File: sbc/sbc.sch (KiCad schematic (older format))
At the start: 15 parts, among them J1 Conn_01x11_Female, J2 Conn_01x11_Female, U1 WD65C02, U2 7400, U3 28C256, U4 HM62256BLP, U5 WD65C22

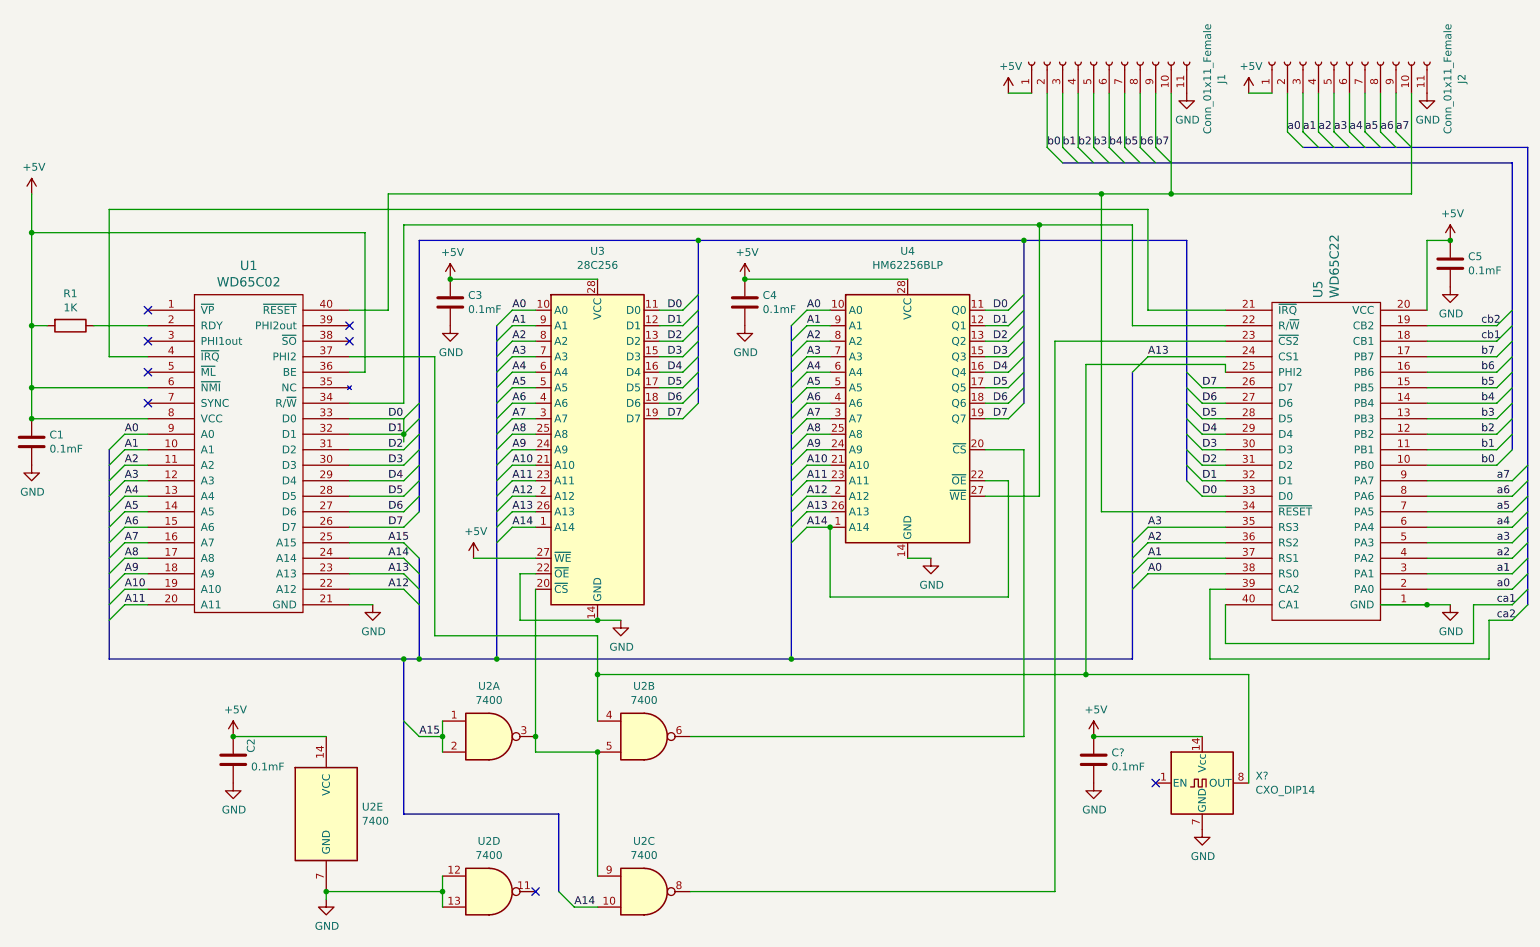
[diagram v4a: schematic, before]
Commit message: SBC: Power and reset
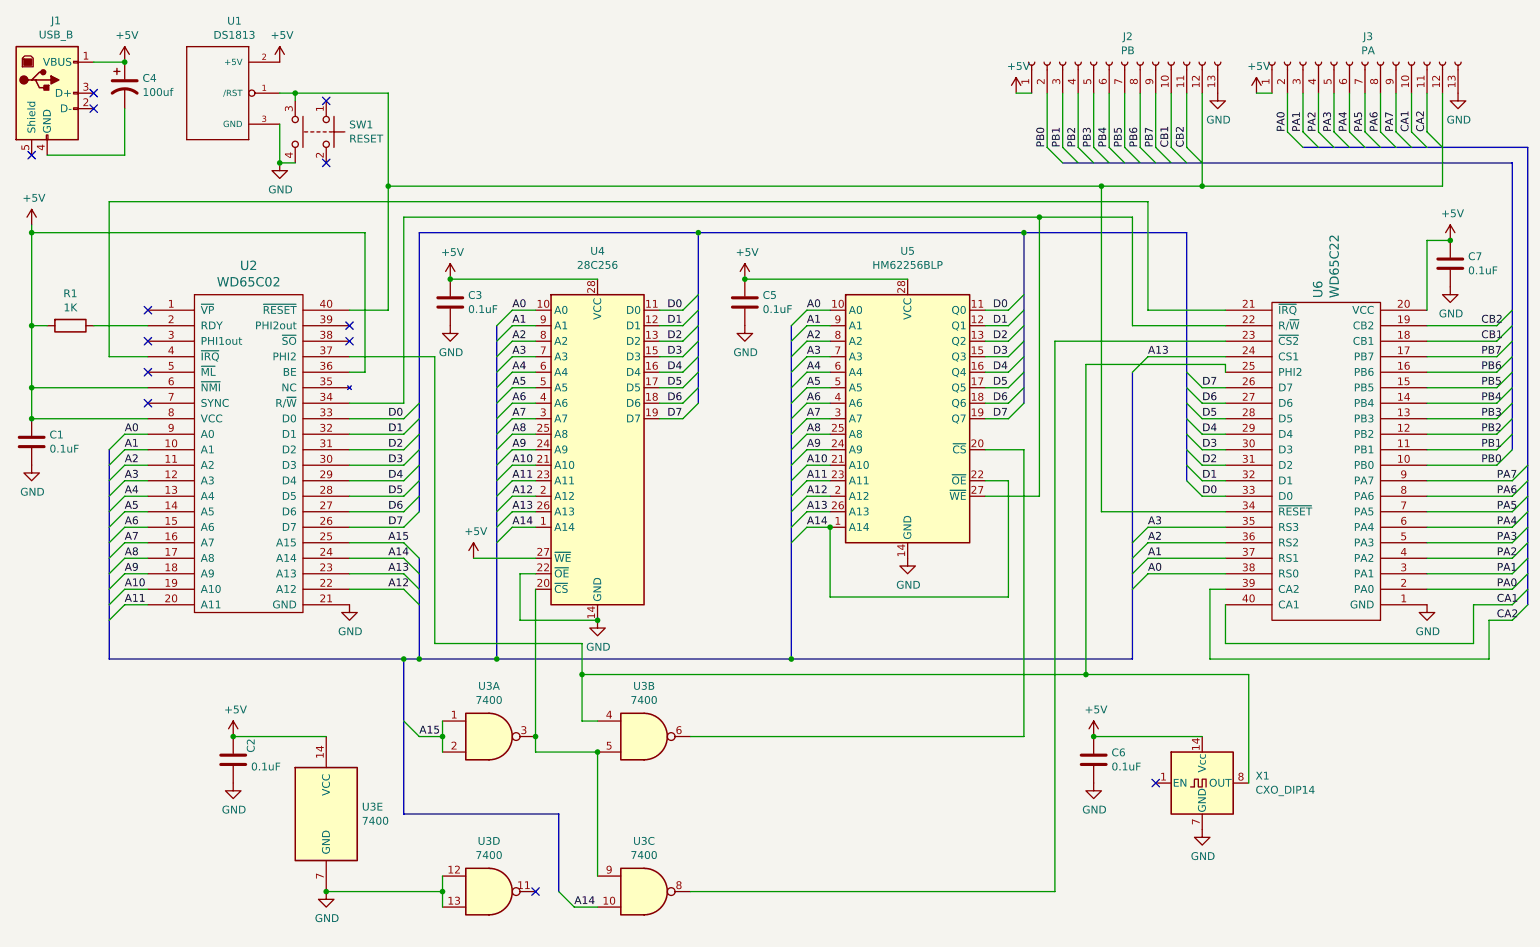
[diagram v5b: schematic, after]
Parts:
- removed J1, J2: Conn_01x11_Female, symbol connector:Conn_01x11_Female
- added C4: 100uf, symbol device:CP1
- added J1: USB_B, symbol connector:USB_B
- added J2: PB, symbol connector:Conn_01x13_Female
- added J3: PA, symbol connector:Conn_01x13_Female
- added SW1: RESET, symbol switch:SW_Push_Dual
- added U1: DS1813, symbol ds1813:DS1813
- C1, C2, C3: value 0.1mF -> 0.1uF
- C5: renamed from C4; value 0.1mF -> 0.1uF
- C6: renamed from C?; value 0.1mF -> 0.1uF
- C7: renamed from C5; value 0.1mF -> 0.1uF
- U5: renamed from U4; footprint Package_DIP:DIP-28_W15.24mm -> (none)
- X1: renamed from X?; footprint Oscillator:Oscillator_DIP-14 -> (none)
- renumbered U1 to U2, U2 to U3, U3 to U4, U5 to U6
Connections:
- net +5V: now also C4.1, J1.1 (VBUS), J2.1 (Pin_1), J3.1 (Pin_1), U1.2 (+5V)
- net D0: no longer U2.32 (D1), U4.12 (D1), U5.12 (Q1), U6.32 (D1)
- net GND: now also J2.13 (Pin_13), J3.13 (Pin_13), SW1.4, U1.3 (GND)
- net at U2.40 (~RESET), U6.34 (~RESET): now also J2.12 (Pin_12), J3.12 (Pin_12), SW1.3, U1.1 (/RST)
- net a0 renamed PA0
- net PA0: now also J3.2 (Pin_2)
- net a1 renamed PA1
- net PA1: now also J3.3 (Pin_3)
- net a2 renamed PA2
- net PA2: now also J3.4 (Pin_4)
- net a3 renamed PA3
- net PA3: now also J3.5 (Pin_5)
- net a4 renamed PA4
- net PA4: now also J3.6 (Pin_6)
- net a5 renamed PA5
- net PA5: now also J3.7 (Pin_7)
- net a6 renamed PA6
- net PA6: now also J3.8 (Pin_8)
- net a7 renamed PA7
- net PA7: now also J3.9 (Pin_9)
- net b0 renamed PB0
- net PB0: now also J2.2 (Pin_2)
- net b1 renamed PB1
- net PB1: now also J2.3 (Pin_3)
- net b2 renamed PB2
- net PB2: now also J2.4 (Pin_4)
- net b3 renamed PB3
- net PB3: now also J2.5 (Pin_5)
- net b4 renamed PB4
- net PB4: now also J2.6 (Pin_6)
- net b5 renamed PB5
- net PB5: now also J2.7 (Pin_7)
- net b6 renamed PB6
- net PB6: now also J2.8 (Pin_8)
- net b7 renamed PB7
- net PB7: now also J2.9 (Pin_9)
- net ca1 renamed CA1
- net CA1: now also J3.10 (Pin_10)
- net ca2 renamed CA2
- net CA2: now also J3.11 (Pin_11)
- net cb1 renamed CB1
- net CB1: now also J2.10 (Pin_10)
- net cb2 renamed CB2
- net CB2: now also J2.11 (Pin_11)
- new net: C4.2, J1.4 (GND)
- new net D1: U2.32 (D1), U4.12 (D1), U5.12 (Q1), U6.32 (D1)
- no-connect marks 8 -> 13

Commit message: SBC: Assign footprints
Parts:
- removed J1: USB_B, symbol connector:USB_B
- added J1: USB_B_Micro, connector_usb:USB_Micro-B_Amphenol_10118194_Horizontal, symbol connector:USB_B_Micro
- C1: renamed from C4; footprint (none) -> capacitor:CP_Radial_D5.0mm_P2.50mm
- C2: renamed from C1; footprint (none) -> capacitor:C_Rect_L4.6mm_W3.0mm_P2.50mm_MKS02_FKP02
- C3: footprint (none) -> capacitor:C_Rect_L4.6mm_W3.0mm_P2.50mm_MKS02_FKP02
- C4: renamed from C5; footprint (none) -> capacitor:C_Rect_L4.6mm_W3.0mm_P2.50mm_MKS02_FKP02
- C5: renamed from C7; footprint (none) -> capacitor:C_Rect_L4.6mm_W3.0mm_P2.50mm_MKS02_FKP02
- C6: renamed from C2; footprint (none) -> capacitor:C_Rect_L4.6mm_W3.0mm_P2.50mm_MKS02_FKP02
- C7: renamed from C6; footprint (none) -> capacitor:C_Rect_L4.6mm_W3.0mm_P2.50mm_MKS02_FKP02
- J2, J3: footprint (none) -> connector:PinSocket_1x13_P2.54mm_Vertical
- R1: footprint (none) -> resistor:R_Axial_DIN0204_L3.6mm_D1.6mm_P5.08mm_Horizontal
- SW1: footprint (none) -> switch:SW_TH_Tactile_Omron_B3F-10xx
- U1: footprint (none) -> to_sot:TO-92_Inline
- U2: footprint (none) -> dip:DIP-40_W15.24mm_Socket
- U3: renamed from U4; footprint (none) -> dip:DIP-28_W15.24mm_Socket
- U4: renamed from U5; footprint (none) -> dip:DIP-28_W15.24mm_Socket
- U5: renamed from U6; footprint (none) -> dip:DIP-40_W15.24mm_Socket
- U6: renamed from U3; footprint (none) -> dip:DIP-14_W7.62mm_Socket
- X1: footprint (none) -> oscillator:Oscillator_DIP-14
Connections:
- net +5V: now also J1.1 (VBUS)
- net at C1.2: now also J1.5 (GND)
- no-connect marks 13 -> 14
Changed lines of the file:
@@
 F 0 "U2" H 2250 4587 60  0000 C CNN
 F 1 "WD65C02" H 2250 4481 60  0000 C CNN
-F 2 "" H 1750 3600 60  0001 C CNN
+F 2 "dip:DIP-40_W15.24mm_Socket" H 1750 3600 60  0001 C CNN
 F 3 "" H 1750 3600 60  0000 C CNN
 	1    2250 3400
@@
 $EndComp
 $Comp
-L eeprom:28C256 U4
+L eeprom:28C256 U3
 U 1 1 6103C55C
 P 4500 3400
-F 0 "U4" H 4500 4681 50  0000 C CNN
+F 0 "U3" H 4500 4681 50  0000 C CNN
 F 1 "28C256" H 4500 4590 50  0000 C CNN
-F 2 "" H 4500 3400 50  0001 C CNN
+F 2 "dip:DIP-28_W15.24mm_Socket" H 4500 3400 50  0001 C CNN
 F 3 "http://ww1.microchip.com/downloads/en/DeviceDoc/doc0006.pdf" H 4500 3400 50  0001 C CNN
 	1    4500 3400
@@
 $EndComp
 $Comp
-L ram:HM62256BLP U5
+L ram:HM62256BLP U4
 U 1 1 6103CC19
 P 6500 3200
-F 0 "U5" H 6500 4281 50  0000 C CNN
+F 0 "U4" H 6500 4281 50  0000 C CNN
 F 1 "HM62256BLP" H 6500 4190 50  0000 C CNN
-F 2 "" H 6500 3100 50  0001 C CNN
+F 2 "dip:DIP-28_W15.24mm_Socket" H 6500 3100 50  0001 C CNN
 F 3 "https://web.mit.edu/6.115/www/document/62256.pdf" H 6500 3100 50  0001 C CNN
 	1    6500 3200
@@
 	1350 4750 3250 4750
 $Comp
-L 74xx:7400 U3
+L 74xx:7400 U6
 U 1 1 61067C42
 P 3800 5250
-F 0 "U3" H 3800 5575 50  0000 C CNN
+F 0 "U6" H 3800 5575 50  0000 C CNN
 F 1 "7400" H 3800 5484 50  0000 C CNN
-F 2 "" H 3800 5250 50  0001 C CNN
+F 2 "dip:DIP-14_W7.62mm_Socket" H 3800 5250 50  0001 C CNN
 F 3 "http://www.ti.com/lit/gpn/sn7400" H 3800 5250 50  0001 C CNN
 	1    3800 5250
@@
 $EndComp
 $Comp
-L 74xx:7400 U3
+L 74xx:7400 U6
 U 2 1 610684A0
 P 4800 5250
-F 0 "U3" H 4800 5575 50  0000 C CNN
+F 0 "U6" H 4800 5575 50  0000 C CNN
 F 1 "7400" H 4800 5484 50  0000 C CNN
-F 2 "" H 4800 5250 50  0001 C CNN
+F 2 "dip:DIP-14_W7.62mm_Socket" H 4800 5250 50  0001 C CNN
 F 3 "http://www.ti.com/lit/gpn/sn7400" H 4800 5250 50  0001 C CNN
 	2    4800 5250
@@
 $EndComp
 $Comp
-L 74xx:7400 U3
+L 74xx:7400 U6
 U 3 1 61069043
 P 4800 6250
-F 0 "U3" H 4800 6575 50  0000 C CNN
+F 0 "U6" H 4800 6575 50  0000 C CNN
 F 1 "7400" H 4800 6484 50  0000 C CNN
-F 2 "" H 4800 6250 50  0001 C CNN
+F 2 "dip:DIP-14_W7.62mm_Socket" H 4800 6250 50  0001 C CNN
 F 3 "http://www.ti.com/lit/gpn/sn7400" H 4800 6250 50  0001 C CNN
 	3    4800 6250
@@
 $EndComp
 $Comp
-L 74xx:7400 U3
+L 74xx:7400 U6
 U 4 1 61069FAE
 P 3800 6250
-F 0 "U3" H 3800 6575 50  0000 C CNN
+F 0 "U6" H 3800 6575 50  0000 C CNN
 F 1 "7400" H 3800 6484 50  0000 C CNN
-F 2 "" H 3800 6250 50  0001 C CNN
+F 2 "dip:DIP-14_W7.62mm_Socket" H 3800 6250 50  0001 C CNN
 F 3 "http://www.ti.com/lit/gpn/sn7400" H 3800 6250 50  0001 C CNN
 	4    3800 6250
@@
 $EndComp
 $Comp
-L 74xx:7400 U3
+L 74xx:7400 U6
 U 5 1 6106B6C1
 P 2750 5750
-F 0 "U3" H 2980 5796 50  0000 L CNN
+F 0 "U6" H 2980 5796 50  0000 L CNN
 F 1 "7400" H 2980 5705 50  0000 L CNN
-F 2 "" H 2750 5750 50  0001 C CNN
+F 2 "dip:DIP-14_W7.62mm_Socket" H 2750 5750 50  0001 C CNN
 F 3 "http://www.ti.com/lit/gpn/sn7400" H 2750 5750 50  0001 C CNN
 	5    2750 5750
@@
 	8400 3000 8300 2900
 $Comp
-L 65xx:WD65C22 U6
+L 65xx:WD65C22 U5
 U 1 1 6104D277
 P 9200 3500
-F 0 "U6" V 9253 2422 60  0000 R CNN
+F 0 "U5" V 9253 2422 60  0000 R CNN
 F 1 "WD65C22" V 9147 2422 60  0000 R CNN
-F 2 "" H 8700 3700 60  0001 C CNN
+F 2 "dip:DIP-40_W15.24mm_Socket" H 8700 3700 60  0001 C CNN
 F 3 "" H 8700 3700 60  0000 C CNN
 	1    9200 3500
@@
 F 0 "R1" V 893 2600 50  0000 C CNN
 F 1 "1K" V 984 2600 50  0000 C CNN
-F 2 "" V 1030 2600 50  0001 C CNN
+F 2 "resistor:R_Axial_DIN0204_L3.6mm_D1.6mm_P5.08mm_Horizontal" V 1030 2600 50  0001 C CNN
 F 3 "~" H 1100 2600 50  0001 C CNN
 	1    1100 2600
@@
 Connection ~ 850  3000
 $Comp
-L device:C C1
+L device:C C2
 U 1 1 610D84A3
 P 850 3350
-F 0 "C1" H 965 3396 50  0000 L CNN
+F 0 "C2" H 965 3396 50  0000 L CNN
 F 1 "0.1uF" H 965 3305 50  0000 L CNN
-F 2 "" H 888 3200 50  0001 C CNN
+F 2 "capacitor:C_Rect_L4.6mm_W3.0mm_P2.50mm_MKS02_FKP02" H 888 3200 50  0001 C CNN
 F 3 "~" H 850 3350 50  0001 C CNN
 	1    850  3350
@@
 F 0 "C3" H 3665 2496 50  0000 L CNN
 F 1 "0.1uF" H 3665 2405 50  0000 L CNN
-F 2 "" H 3588 2300 50  0001 C CNN
+F 2 "capacitor:C_Rect_L4.6mm_W3.0mm_P2.50mm_MKS02_FKP02" H 3588 2300 50  0001 C CNN
 F 3 "~" H 3550 2450 50  0001 C CNN
 	1    3550 2450
@@
 $EndComp
 $Comp
-L device:C C5
+L device:C C4
 U 1 1 6118D18B
 P 5450 2450
-F 0 "C5" H 5565 2496 50  0000 L CNN
+F 0 "C4" H 5565 2496 50  0000 L CNN
 F 1 "0.1uF" H 5565 2405 50  0000 L CNN
-F 2 "" H 5488 2300 50  0001 C CNN
+F 2 "capacitor:C_Rect_L4.6mm_W3.0mm_P2.50mm_MKS02_FKP02" H 5488 2300 50  0001 C CNN
 F 3 "~" H 5450 2450 50  0001 C CNN
 	1    5450 2450
@@
 $EndComp
 $Comp
-L device:C C7
+L device:C C5
 U 1 1 611EFCC9
 P 10000 2200
-F 0 "C7" H 10115 2246 50  0000 L CNN
+F 0 "C5" H 10115 2246 50  0000 L CNN
 F 1 "0.1uF" H 10115 2155 50  0000 L CNN
-F 2 "" H 10038 2050 50  0001 C CNN
+F 2 "capacitor:C_Rect_L4.6mm_W3.0mm_P2.50mm_MKS02_FKP02" H 10038 2050 50  0001 C CNN
 F 3 "~" H 10000 2200 50  0001 C CNN
 	1    10000 2200
@@
 	3450 4650 3450 2800
 $Comp
-L device:C C2
+L device:C C6
 U 1 1 610A0E68
 P 2150 5400
-F 0 "C2" V 2265 5446 50  0000 L CNN
+F 0 "C6" V 2265 5446 50  0000 L CNN
 F 1 "0.1uF" H 2265 5355 50  0000 L CNN
-F 2 "" H 2188 5250 50  0001 C CNN
+F 2 "capacitor:C_Rect_L4.6mm_W3.0mm_P2.50mm_MKS02_FKP02" H 2188 5250 50  0001 C CNN
 F 3 "~" H 2150 5400 50  0001 C CNN
 	1    2150 5400
@@
 F 0 "X1" H 8744 5596 50  0000 L CNN
 F 1 "CXO_DIP14" H 8744 5505 50  0000 L CNN
-F 2 "" H 8850 5200 50  0001 C CNN
+F 2 "oscillator:Oscillator_DIP-14" H 8850 5200 50  0001 C CNN
 F 3 "http://cdn-reichelt.de/documents/datenblatt/B400/OSZI.pdf" H 8300 5550 50  0001 C CNN
 	1    8400 5550
@@
 $EndComp
 $Comp
-L device:C C6
+L device:C C7
 U 1 1 6119EE14
 P 7700 5400
-F 0 "C6" H 7815 5446 50  0000 L CNN
+F 0 "C7" H 7815 5446 50  0000 L CNN
 F 1 "0.1uF" H 7815 5355 50  0000 L CNN
-F 2 "" H 7738 5250 50  0001 C CNN
+F 2 "capacitor:C_Rect_L4.6mm_W3.0mm_P2.50mm_MKS02_FKP02" H 7738 5250 50  0001 C CNN
 F 3 "~" H 7700 5400 50  0001 C CNN
 	1    7700 5400
@@
 F 0 "J2" V 8065 880 50  0000 C CNN
 F 1 "PB" V 7974 880 50  0000 C CNN
-F 2 "" H 7900 900 50  0001 C CNN
+F 2 "connector:PinSocket_1x13_P2.54mm_Vertical" H 7900 900 50  0001 C CNN
 F 3 "~" H 7900 900 50  0001 C CNN
 	1    7900 900
@@
 F 0 "J3" V 9615 880 50  0000 C CNN
 F 1 "PA" V 9524 880 50  0000 C CNN
-F 2 "" H 9450 900 50  0001 C CNN
+F 2 "connector:PinSocket_1x13_P2.54mm_Vertical" H 9450 900 50  0001 C CNN
 F 3 "~" H 9450 900 50  0001 C CNN
 	1    9450 900
@@
 F 0 "U1" H 2158 1565 50  0000 C CNN
 F 1 "DS1813" H 2158 1474 50  0000 C CNN
-F 2 "" H 1950 1250 50  0001 C CNN
+F 2 "to_sot:TO-92_Inline" H 1950 1250 50  0001 C CNN
 F 3 "" H 1950 1100 50  0001 C CNN
 	1    1950 1100
@@
 F 0 "SW1" V 2704 1498 50  0000 L CNN
 F 1 "RESET" V 2795 1498 50  0000 L CNN
-F 2 "" H 2750 1550 50  0001 C CNN
+F 2 "switch:SW_TH_Tactile_Omron_B3F-10xx" H 2750 1550 50  0001 C CNN
 F 3 "~" H 2750 1550 50  0001 C CNN
 	1    2750 1350
@@
 NoConn ~ 1250 1100
 $Comp
-L connector:USB_B J1
-U 1 1 6136DFC7
-P 950 1100
-F 0 "J1" H 1007 1567 50  0000 C CNN
-F 1 "USB_B" H 1007 1476 50  0000 C CNN
-F 2 "" H 1100 1050 50  0001 C CNN
-F 3 " ~" H 1100 1050 50  0001 C CNN
-	1    950  1100
-	1    0    0    -1
-$EndComp
-$Comp
-L device:CP1 C4
+L device:CP1 C1
 U 1 1 610C6BA6
 P 1450 1050
-F 0 "C4" H 1565 1096 50  0000 L CNN
+F 0 "C1" H 1565 1096 50  0000 L CNN
 F 1 "100uf" H 1565 1005 50  0000 L CNN
-F 2 "" H 1450 1050 50  0001 C CNN
+F 2 "capacitor:CP_Radial_D5.0mm_P2.50mm" H 1450 1050 50  0001 C CNN
 F 3 "~" H 1450 1050 50  0001 C CNN
 	1    1450 1050
@@
 $EndComp
 Connection ~ 1450 900
+$Comp
+L connector:USB_B_Micro J1
+U 1 1 61270BB5
+P 950 1100
+F 0 "J1" H 1007 1567 50  0000 C CNN
+F 1 "USB_B_Micro" H 1007 1476 50  0000 C CNN
+F 2 "connector_usb:USB_Micro-B_Amphenol_10118194_Horizontal" H 1100 1050 50  0001 C CNN
+F 3 "~" H 1100 1050 50  0001 C CNN
+	1    950  1100
+	1    0    0    -1
+$EndComp
+NoConn ~ 1250 1300
 Wire Wire Line
 	9950 1100 9950 1700

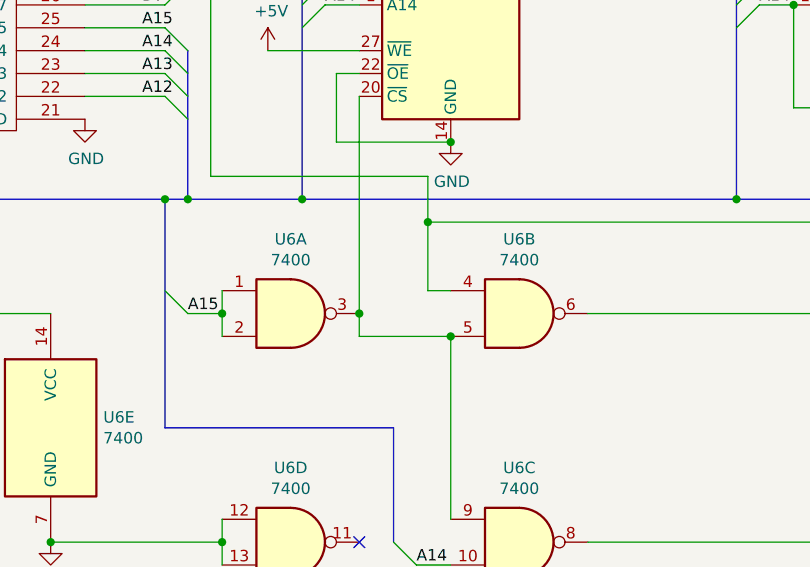
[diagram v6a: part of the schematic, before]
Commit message: SBC: Wire up memories
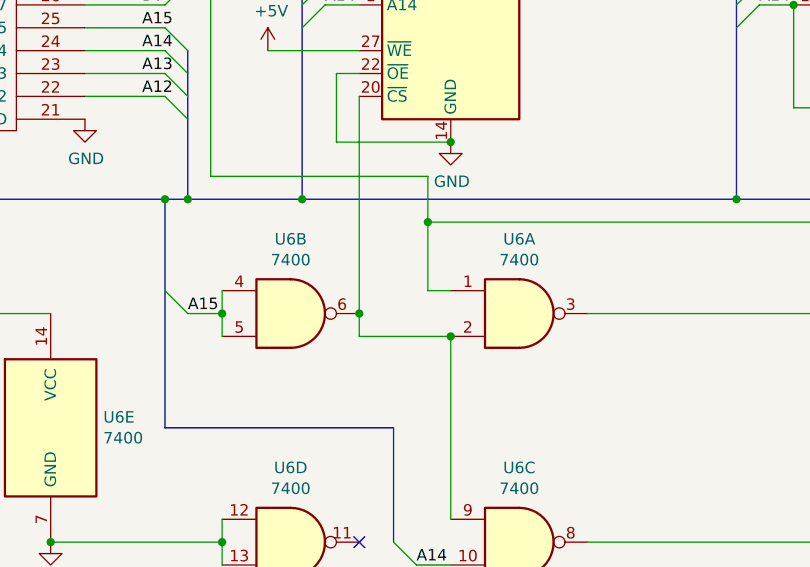
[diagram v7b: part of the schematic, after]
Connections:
- net A15: now also U6.4, U6.5; no longer U6.1, U6.2
- net at U2.37 (PHI2), U5.25 (PHI2), X1.8 (OUT): now also U6.1; no longer U6.4
- net at U3.20 (~CS), U6.9: now also U6.2, U6.6; no longer U6.3, U6.5
- net at U4.20 (~CS): now also U6.3; no longer U6.6
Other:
- moved on the sheet: U6A, U6B
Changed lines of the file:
@@
 L 74xx:7400 U6
 U 1 1 61067C42
+P 4800 5250
+F 0 "U6" H 4800 5575 50  0000 C CNN
+F 1 "7400" H 4800 5484 50  0000 C CNN
+F 2 "dip:DIP-14_W7.62mm_Socket" H 4800 5250 50  0001 C CNN
+F 3 "http://www.ti.com/lit/gpn/sn7400" H 4800 5250 50  0001 C CNN
+	1    4800 5250
+	1    0    0    -1
+$EndComp
+$Comp
+L 74xx:7400 U6
+U 2 1 610684A0
 P 3800 5250
 F 0 "U6" H 3800 5575 50  0000 C CNN
@@
 F 2 "dip:DIP-14_W7.62mm_Socket" H 3800 5250 50  0001 C CNN
 F 3 "http://www.ti.com/lit/gpn/sn7400" H 3800 5250 50  0001 C CNN
-	1    3800 5250
+	2    3800 5250
 	1    0    0    -1
 $EndComp
-$Comp
-L 74xx:7400 U6
-U 2 1 610684A0
-P 4800 5250
-F 0 "U6" H 4800 5575 50  0000 C CNN
-F 1 "7400" H 4800 5484 50  0000 C CNN
-F 2 "dip:DIP-14_W7.62mm_Socket" H 4800 5250 50  0001 C CNN
-F 3 "http://www.ti.com/lit/gpn/sn7400" H 4800 5250 50  0001 C CNN
-	2    4800 5250
-	1    0    0    -1
-$EndComp
